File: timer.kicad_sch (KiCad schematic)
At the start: 30 parts, among them SW1 reset_btn, SW2 start_stop_btn, SW3 A7D-206-1, SW4 A7D-206-1, SW5 A7D-206-1, SW6 A7D-206-1, U1 OSL-40391-LX, U2 74HC595, U3 74HC165, U4 74HC165, U5 74HC00

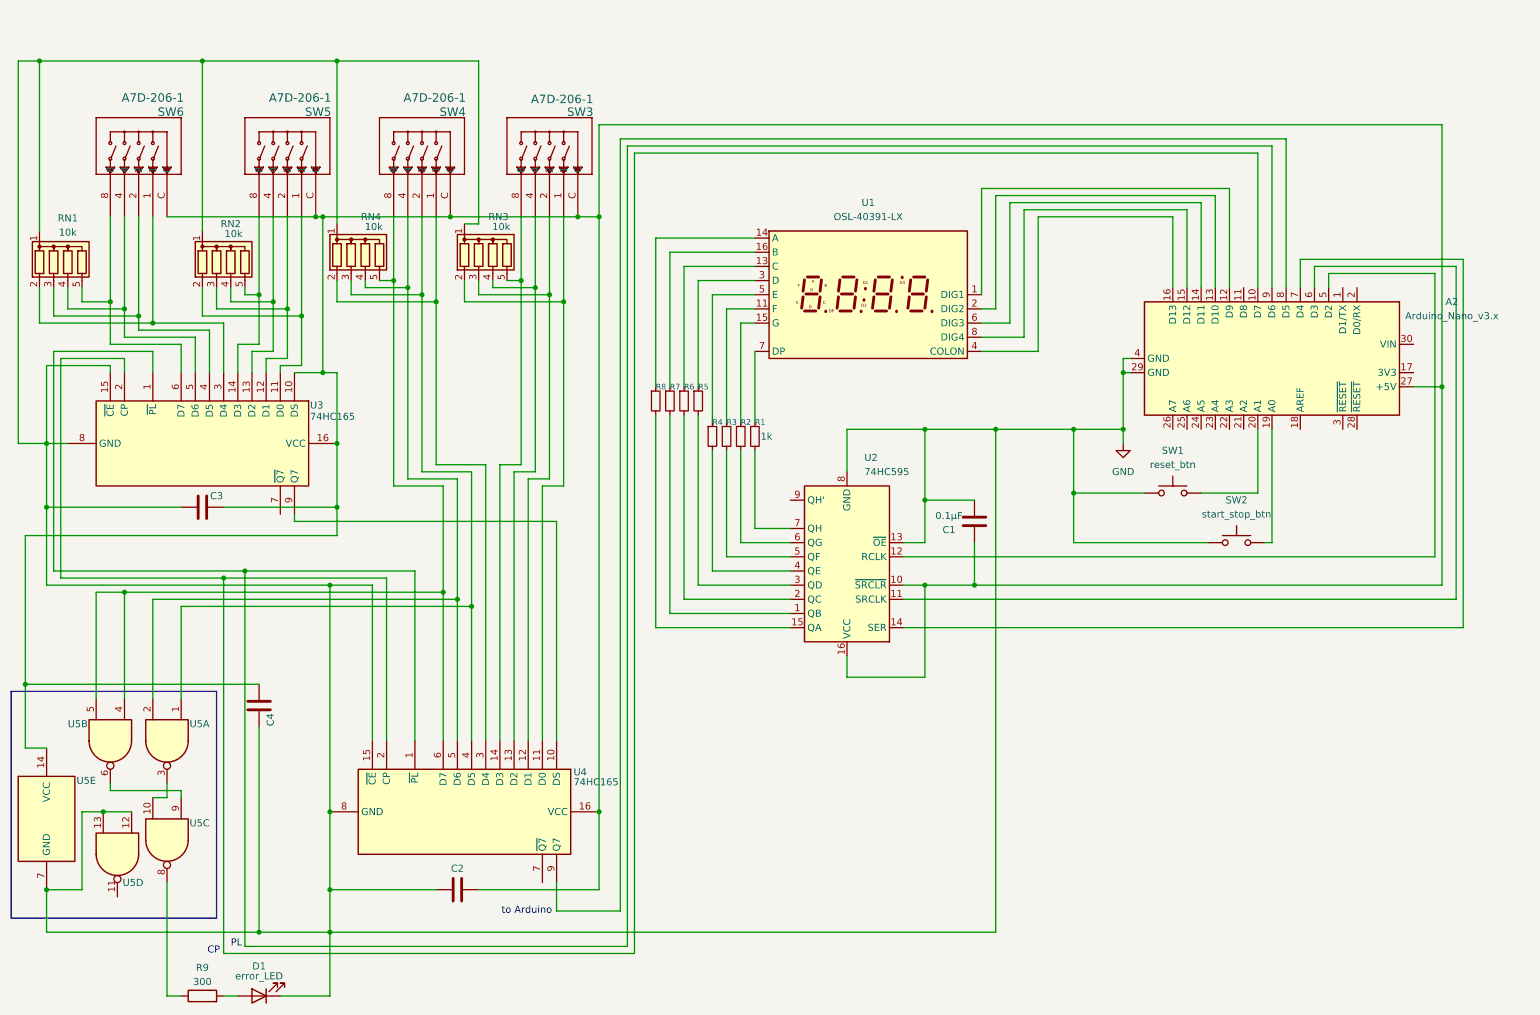
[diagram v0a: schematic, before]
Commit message: feat: タクトスイッチのデバウンスとタイマー状態保持回路を追加
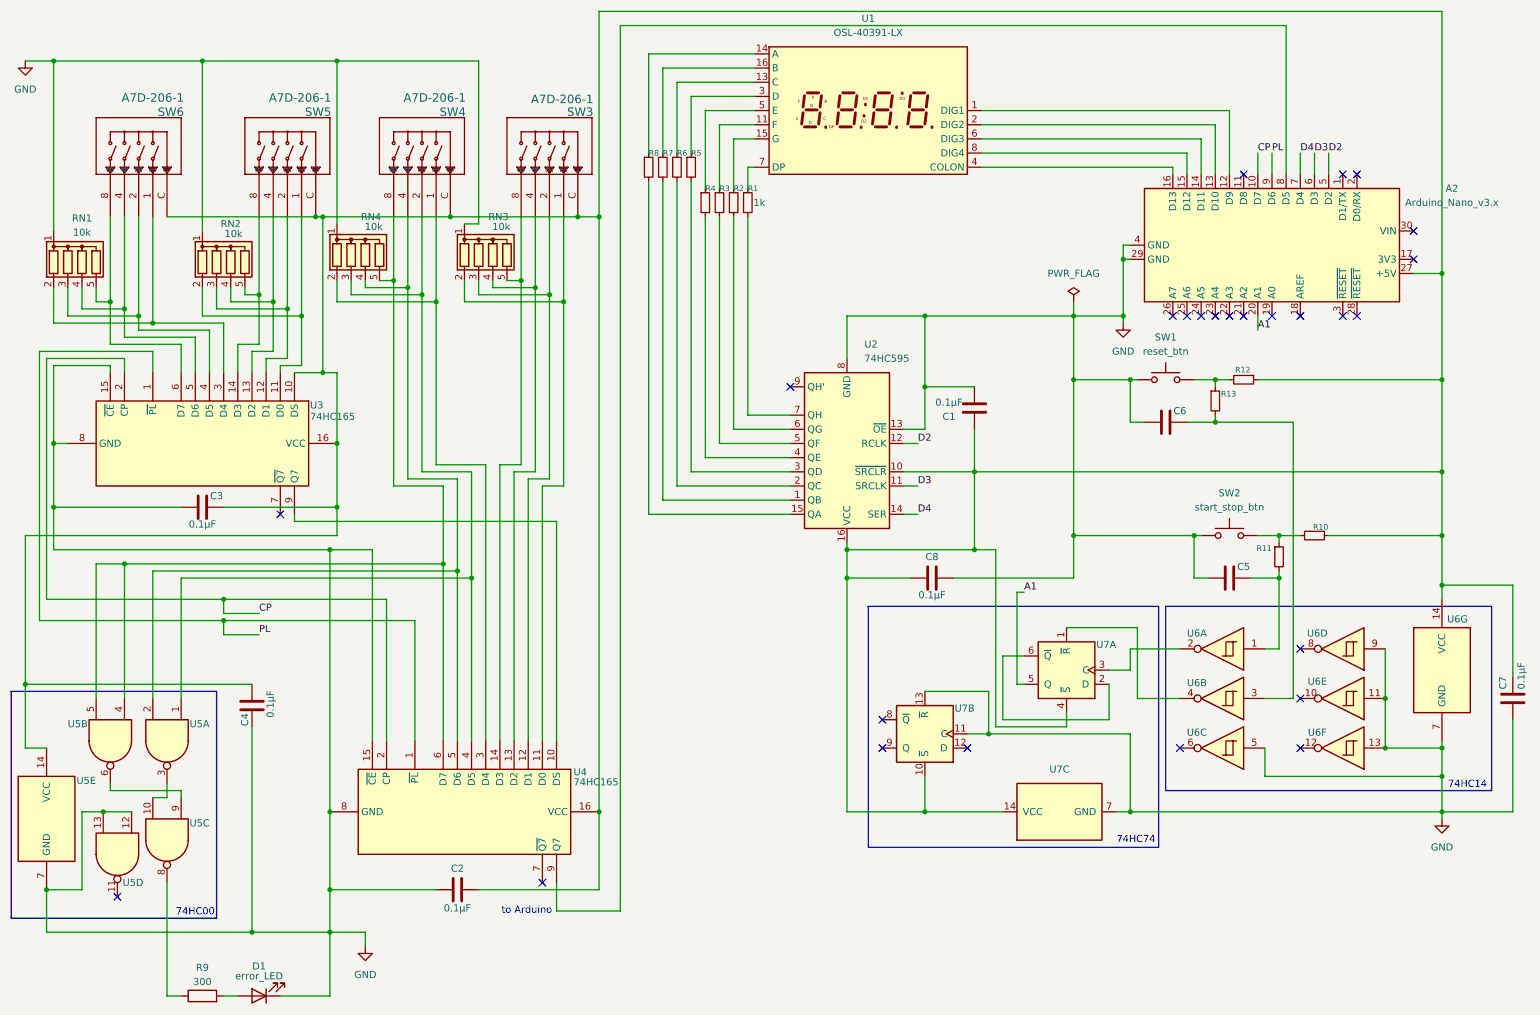
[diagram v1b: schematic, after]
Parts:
- added C5, C6, C7, C8: 0.1μF, Capacitor_THT:C_Disc_D5.0mm_W2.5mm_P5.00mm, symbol Device:C
- added R10, R11, R12, R13: 1k, Resistor_THT:R_Axial_DIN0207_L6.3mm_D2.5mm_P10.16mm_Horizontal, symbol Device:R_Small
- added U6: 74HC14, symbol 74xx:74HC14
- added U7: 74HC74, symbol 74xx:74HC74
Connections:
- net GND: now also C5.1, C6.1, C7.1, C8.2, U6.11, U6.13, U6.5, U6.7 (GND), U6.9, U7.11 (C), U7.13 (~{R}), U7.7 (GND)
- net at A2.27 (+5V), C1.1, C2.2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: now also C7.2, C8.1, R10.1, R12.1, U6.14 (VCC), U7.10 (~{S}), U7.14 (VCC), U7.4 (~{S})
- net D3: now reaches A2.6 (D3), U2.11 (SRCLK)
- net D2: now reaches A2.5 (D2), U2.12 (RCLK)
- net D4: now reaches A2.7 (D4), U2.14 (SER)
- net PL: now reaches A2.9 (D6), U3.1 (~{PL}), U4.1 (~{PL})
- net CP: now reaches A2.10 (D7), U3.2 (CP), U4.2 (CP)
- net at SW2.2: now also R10.2, R11.1; no longer A2.19 (A0)
- net at SW1.2: now also R12.2, R13.1; no longer A2.20 (A1)
- new net: C5.2, R11.2, U6.1
- new net: C6.2, R13.2, U6.3
- new net: U6.2, U7.3 (C)
- new net: U6.4, U7.1 (~{R})
- new net: U7.2 (D), U7.6 (~{Q})
- new net A1: A2.20 (A1), U7.5 (Q)
- no-connect marks 0 -> 26
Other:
- note added: "74HC00"
- note added: "74HC14"
- note added: "74HC74"
- note removed: "CP"
- note removed: "PL"
- moved on the sheet: A2, C1, C4, R1, R2, R3, R4, R5, R6, R7, R8, RN1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

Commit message: feat: ブザーを追加
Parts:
- added BZ1: Buzzer, symbol Device:Buzzer
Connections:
- net GND: now also BZ1.2 (-)
- net at A2.26 (A7): now also BZ1.1 (+)
- no-connect marks 26 -> 25
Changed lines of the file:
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@@
 	)
 	(junction
+		(at 212.09 55.88)
+		(diameter 0)
+		(color 0 0 0 0)
+	)
+	(junction
 		(at 212.09 58.42)
 		(diameter 0)
@@
 	)
 	(no_connect
-		(at 264.16 53.34)
-	)
-	(no_connect
 		(at 264.16 58.42)
 	)
 	(no_connect
-		(at 220.98 68.58)
+		(at 264.16 53.34)
 	)
 	(no_connect
@@
 	(wire
 		(pts
+			(xy 236.22 68.58) (xy 236.22 72.39)
+		)
+		(stroke
+			(width 0)
+			(type default)
+		)
+	)
+	(wire
+		(pts
 			(xy 190.5 129.54) (xy 190.5 140.97)
 		)
@@
 	(wire
 		(pts
+			(xy 212.09 55.88) (xy 213.36 55.88)
+		)
+		(stroke
+			(width 0)
+			(type default)
+		)
+	)
+	(wire
+		(pts
 			(xy 71.12 78.74) (xy 71.12 91.44)
 		)
@@
 	(wire
 		(pts
+			(xy 205.74 52.07) (xy 205.74 55.88)
+		)
+		(stroke
+			(width 0)
+			(type default)
+		)
+	)
+	(wire
+		(pts
 			(xy 48.26 71.12) (xy 35.56 71.12)
 		)
@@
 	(wire
 		(pts
+			(xy 205.74 55.88) (xy 212.09 55.88)
+		)
+		(stroke
+			(width 0)
+			(type default)
+		)
+	)
+	(wire
+		(pts
 			(xy 46.99 22.86) (xy 71.12 22.86)
 		)
@@
 	(wire
 		(pts
+			(xy 220.98 68.58) (xy 214.63 68.58)
+		)
+		(stroke
+			(width 0)
+			(type default)
+		)
+	)
+	(wire
+		(pts
 			(xy 236.22 39.37) (xy 236.22 43.18)
 		)
@@
 	(wire
 		(pts
+			(xy 214.63 68.58) (xy 214.63 59.69)
+		)
+		(stroke
+			(width 0)
+			(type default)
+		)
+	)
+	(wire
+		(pts
 			(xy 142.24 50.8) (xy 142.24 88.9)
 		)
@@
 	(wire
 		(pts
+			(xy 200.66 59.69) (xy 200.66 52.07)
+		)
+		(stroke
+			(width 0)
+			(type default)
+		)
+	)
+	(wire
+		(pts
 			(xy 86.36 50.8) (xy 86.36 64.77)
 		)
@@
 	(wire
 		(pts
+			(xy 214.63 59.69) (xy 200.66 59.69)
+		)
+		(stroke
+			(width 0)
+			(type default)
+		)
+	)
+	(wire
+		(pts
 			(xy 40.64 152.4) (xy 40.64 154.94)
 		)
@@
 	(wire
 		(pts
-			(xy 236.22 68.58) (xy 236.22 71.12)
-		)
-		(stroke
-			(width 0)
-			(type default)
-		)
-	)
-	(wire
-		(pts
 			(xy 20.32 53.34) (xy 20.32 22.86)
 		)
@@
 	(wire
 		(pts
-			(xy 213.36 55.88) (xy 212.09 55.88)
-		)
-		(stroke
-			(width 0)
-			(type default)
-		)
-	)
-	(wire
-		(pts
 			(xy 71.12 62.23) (xy 71.12 66.04)
 		)
@@
 	)
 	(label "A1"
-		(at 236.22 71.12 0)
+		(at 236.22 72.39 0)
 		(effects
 			(font
@@
 					(unit 1)
 				)
+			)
+		)
+	)
+	(symbol
+		(lib_id "Device:Buzzer")
+		(at 203.2 49.53 90)
+		(unit 1)
+		(body_style 1)
+		(exclude_from_sim no)
+		(in_bom yes)
+		(on_board yes)
+		(in_pos_files yes)
+		(dnp no)
+		(fields_autoplaced yes)
+		(property "Reference" "BZ1"
+			(at 207.01 47.5048 90)
+			(show_name no)
+			(do_not_autoplace no)
+			(effects
+				(font
+					(size 1.27 1.27)
+				)
+				(justify right)
+			)
+		)
+		(property "Value" "Buzzer"
+			(at 207.01 50.0448 90)
+			(show_name no)
+			(do_not_autoplace no)
+			(effects
+				(font
+					(size 1.27 1.27)
+				)
+				(justify right)
+			)
+		)
+		(property "Footprint" ""
+			(at 200.66 50.165 90)
+			(hide yes)
+			(show_name no)
+			(do_not_autoplace no)
+			(effects
+				(font
+					(size 1.27 1.27)
+				)
+			)
+		)
+		(property "Datasheet" ""
+			(at 200.66 50.165 90)
+			(hide yes)
+			(show_name no)
+			(do_not_autoplace no)
+			(effects
+				(font
+					(size 1.27 1.27)
+				)
+			)
+		)
+		(property "Description" "Buzzer, polarized"
+			(at 203.2 49.53 0)
+			(hide yes)
+			(show_name no)
+			(do_not_autoplace no)
+			(effects
+				(font
+					(size 1.27 1.27)
+				)
+			)
+		)
+		(pin "1"
+		)
+		(pin "2"
+		)
+		(instances
+			(project "timer"
+				(path "/d75631b8-0d07-44dd-83d0-e59206b11940"
+					(reference "BZ1")
+					(unit 1)
+				)

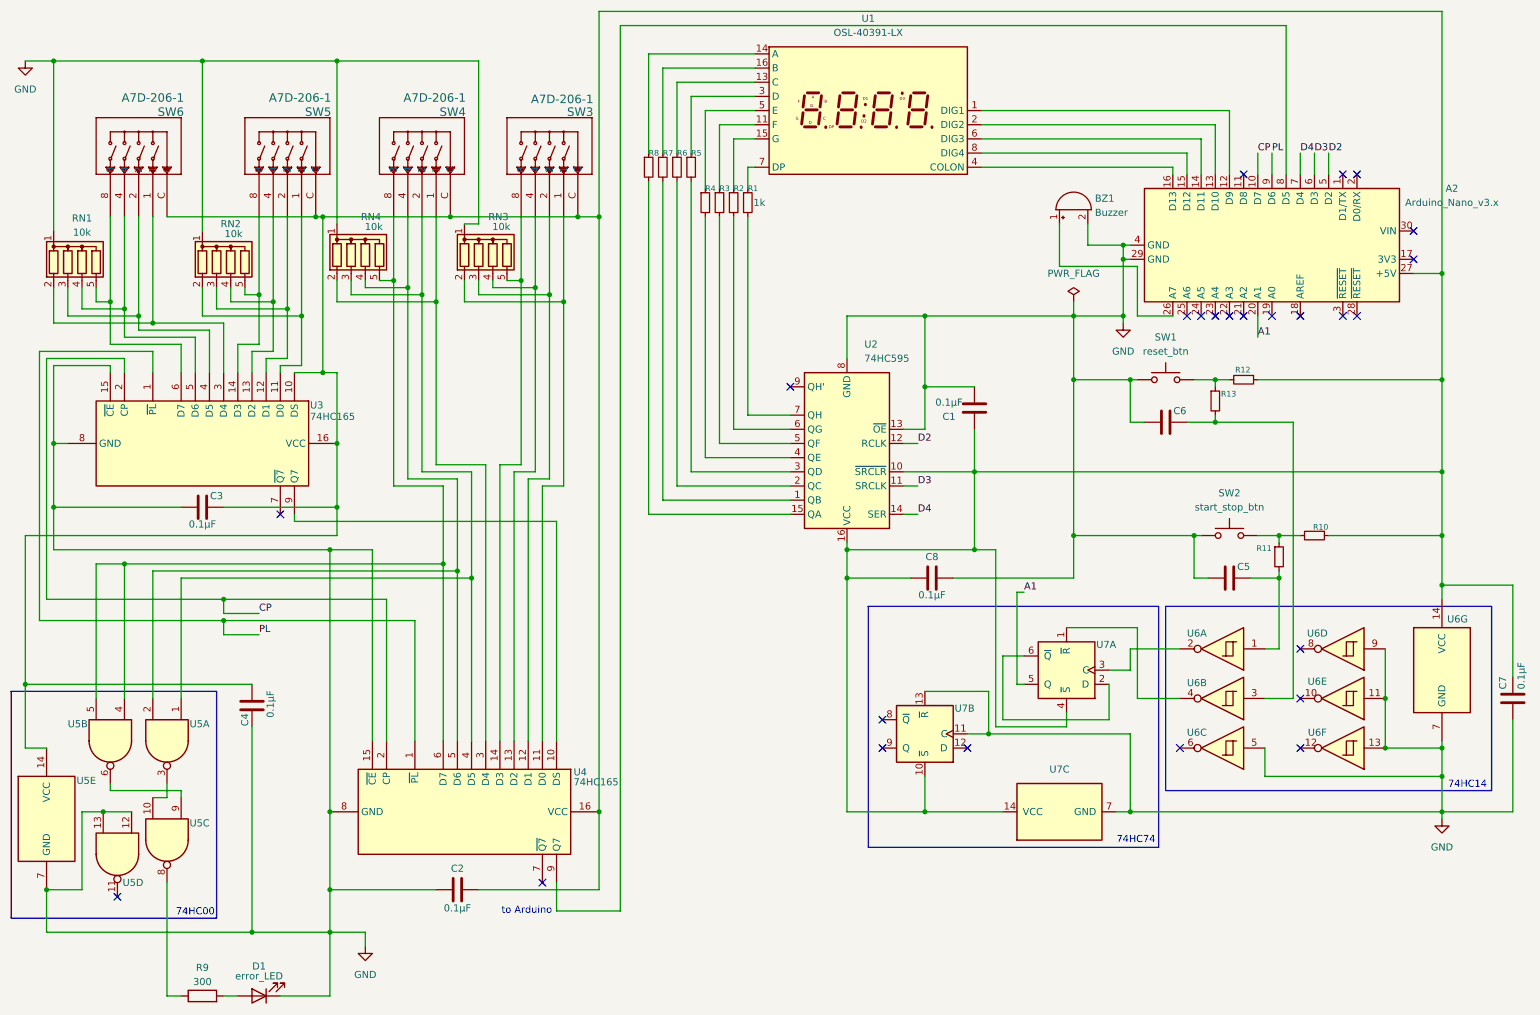
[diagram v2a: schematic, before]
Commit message: feat: クロック・カウンタ回路を追加
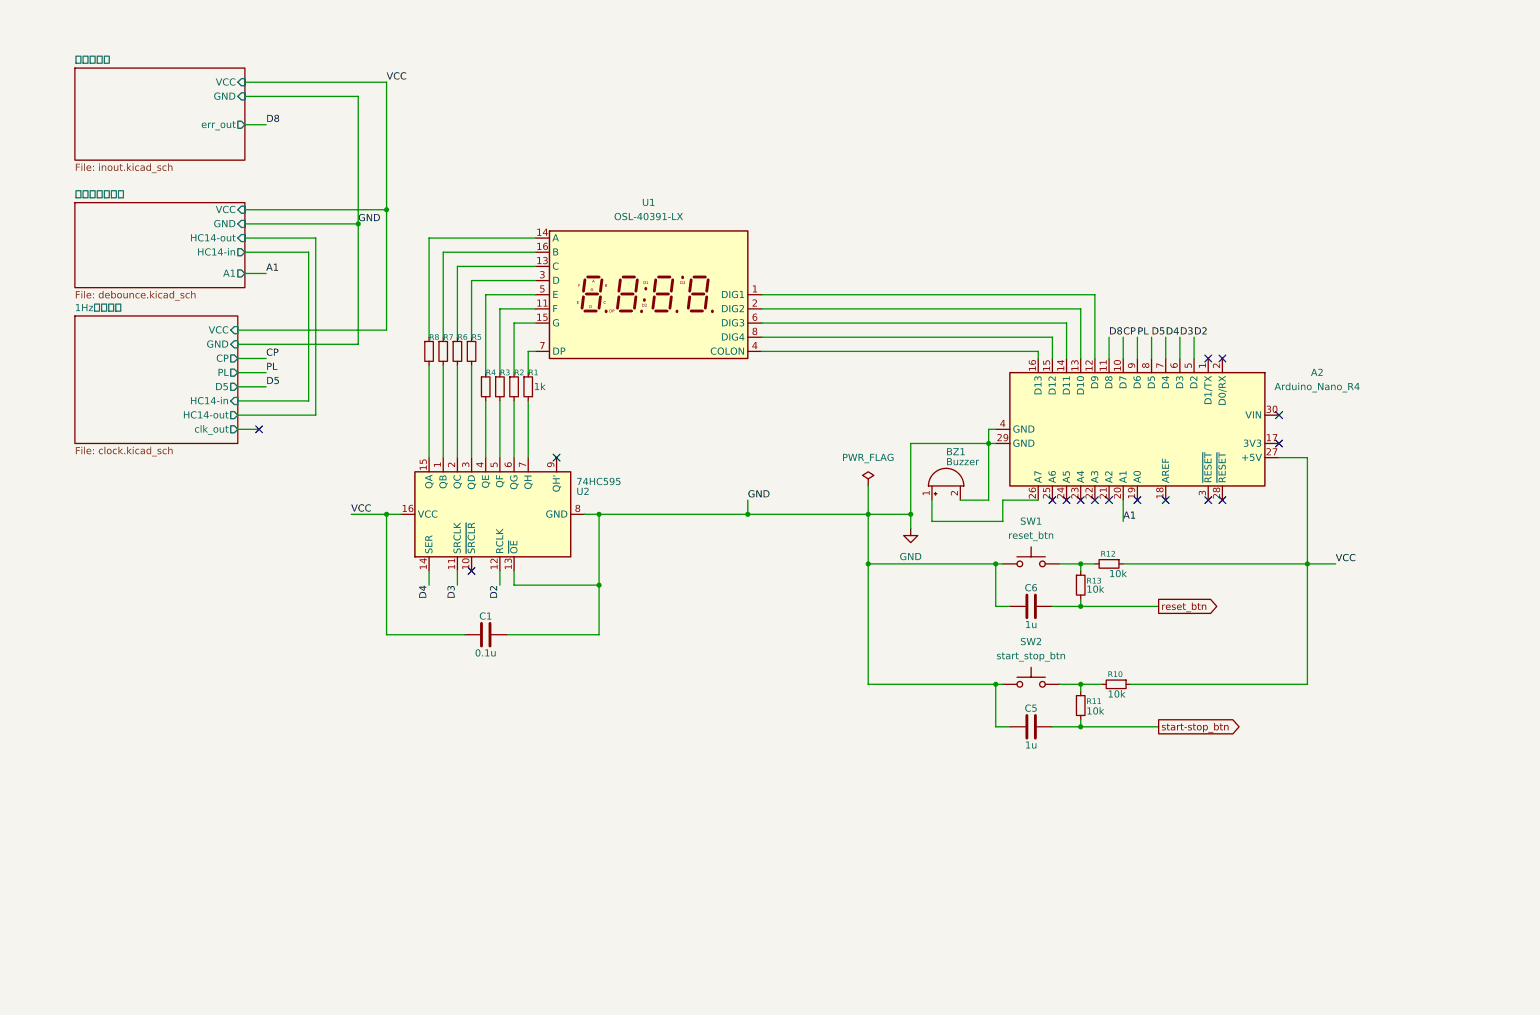
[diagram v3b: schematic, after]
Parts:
- removed C2, C3, C4, C7, C8: 0.1μF, Capacitor_THT:C_Disc_D5.0mm_W2.5mm_P5.00mm, symbol Device:C
- removed D1: error_LED, LED_THT:LED_D3.0mm, symbol Device:LED
- removed R9: 300, Resistor_THT:R_Axial_DIN0207_L6.3mm_D2.5mm_P10.16mm_Horizontal, symbol Device:R
- removed RN1, RN2, RN3, RN4: 10k, Resistor_THT:R_Array_SIP5, symbol Device:R_Network04
- removed SW3, SW4, SW5, SW6: A7D-206-1, mylibraly:A7D-206-1_OMR, symbol my_Library:A7D-206-1
- removed U3, U4: 74HC165, Package_DIP:DIP-16_W7.62mm_Socket, symbol 74xx:74HC165
- removed U5: 74HC00, Package_DIP:DIP-14_W7.62mm_Socket, symbol 74xx:74HC00
- removed U6: 74HC14, symbol 74xx:74HC14
- removed U7: 74HC74, symbol 74xx:74HC74
- A2: value Arduino_Nano_v3.x -> Arduino_Nano_R4
- BZ1: footprint (none) -> Buzzer_Beeper:Buzzer_12x9.5RM7.6
- C1: value 0.1μF -> 0.1u
- C5, C6: value 0.1μF -> 1u
- R10, R11, R12, R13: value 1k -> 10k
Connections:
- net VCC: now reaches A2.27 (+5V), C1.1, R10.1, R12.1, U2.16 (VCC)
- net VCC: no longer U2.10 (~{SRCLR})
- net start-stop_btn: now reaches C5.2, R11.2
- net D5: now reaches A2.8 (D5)
- net reset_btn: now reaches C6.2, R13.2
- net D8: now reaches A2.11 (D8)
- no-connect marks 25 -> 16
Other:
- added sheet 1Hz発振回路 (clock.kicad_sch)
- added sheet デバウンス回路 (debounce.kicad_sch)
- added sheet 時間入力部 (inout.kicad_sch)
- note removed: "74HC00"
- note removed: "74HC14"
- note removed: "74HC74"
- note removed: "to Arduino"
- moved on the sheet: A2, BZ1, C5, C6, R1, R10, R11, R12, R13, R2, R3, R4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

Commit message: feat: クロック回路にデカップリングコンデンサを追加
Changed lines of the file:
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@@
 			)
 		)
-		(pin "HC14-in" input
+		(pin "HC14-in" output
 			(at 53.34 83.82 0)
 			(effects
@@
 			)
 		)
-		(pin "HC14-out" output
+		(pin "HC14-out" input
 			(at 53.34 86.36 0)
 			(effects
